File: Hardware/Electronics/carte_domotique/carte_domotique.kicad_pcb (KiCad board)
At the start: 2 copper layers, 27.9 x 58.4 mm, 3 parts, among them J1 Conn_02x08_Counter_Clockwise, J2 Raspberry_Pi_2_3, J3 Conn_01x02

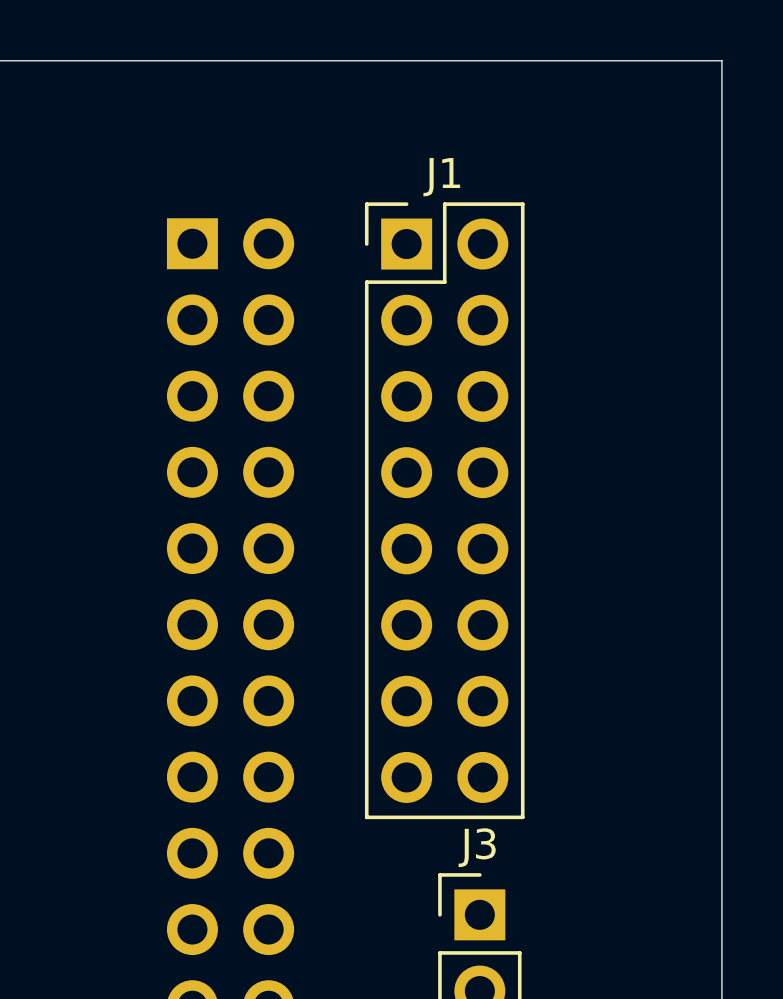
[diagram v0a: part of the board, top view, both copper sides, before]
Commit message: motification du conneteur pour le raspbee II
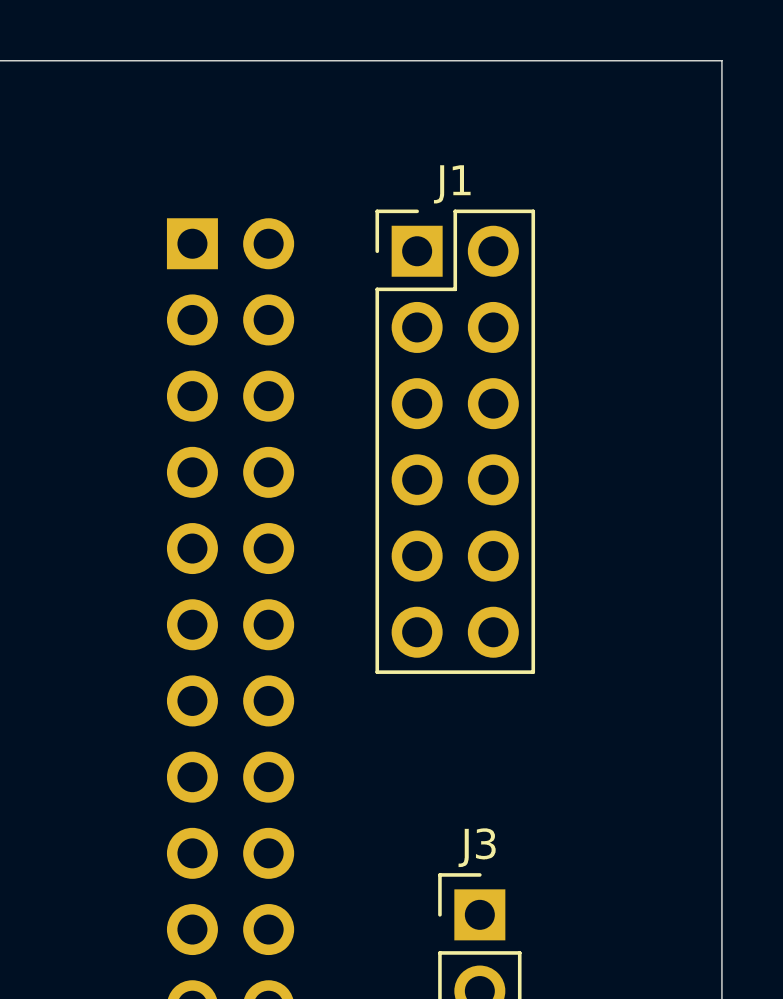
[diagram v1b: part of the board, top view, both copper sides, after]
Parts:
- J1: value Conn_02x08_Counter_Clockwise -> Conn_02x06_Odd_Even; footprint Connector_PinHeader_2.54mm:PinHeader_2x08_P2.54mm_Vertical -> Connector_PinHeader_2.54mm:PinHeader_2x06_P2.54mm_Vertical
- moved J1 0.42 mm to (147.3, 39.4)
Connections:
- J1 pad 5: Net-(J1-Pad10) -> Net-(J1-Pad5)
- J2 pad 10: Net-(J1-Pad12) -> Net-(J1-Pad10)
- J2 pad 11: Net-(J1-Pad6) -> Net-(J1-Pad11)
- J2 pad 12: Net-(J1-Pad11) -> Net-(J1-Pad12)
- J2 pad 13: Net-(J1-Pad7) -> Net-(J2-Pad13)
- J2 pad 14: Net-(J1-Pad10) -> Net-(J1-Pad9)
- J2 pad 15: Net-(J1-Pad8) -> Net-(J2-Pad15)
- J2 pad 16: Net-(J1-Pad9) -> Net-(J2-Pad16)
- J2 pad 2: Net-(J1-Pad15) -> Net-(J1-Pad2)
- J2 pad 20: Net-(J1-Pad10) -> Net-(J1-Pad9)
- J2 pad 25: Net-(J1-Pad10) -> Net-(J1-Pad9)
- J2 pad 3: Net-(J1-Pad2) -> Net-(J1-Pad3)
- J2 pad 30: Net-(J1-Pad10) -> Net-(J1-Pad9)
- J2 pad 34: Net-(J1-Pad10) -> Net-(J1-Pad9)
- J2 pad 39: Net-(J1-Pad10) -> Net-(J1-Pad9)
- J2 pad 4: Net-(J1-Pad15) -> Net-(J1-Pad2)
- J2 pad 5: Net-(J1-Pad3) -> Net-(J1-Pad5)
- J2 pad 6: Net-(J1-Pad10) -> Net-(J1-Pad9)
- J2 pad 7: Net-(J1-Pad4) -> Net-(J1-Pad7)
- J2 pad 8: Net-(J1-Pad13) -> Net-(J1-Pad8)
- J2 pad 9: Net-(J1-Pad10) -> Net-(J1-Pad9)
- J3 pad 1: Net-(J1-Pad15) -> Net-(J1-Pad2)
- J3 pad 2: Net-(J1-Pad10) -> Net-(J1-Pad6)

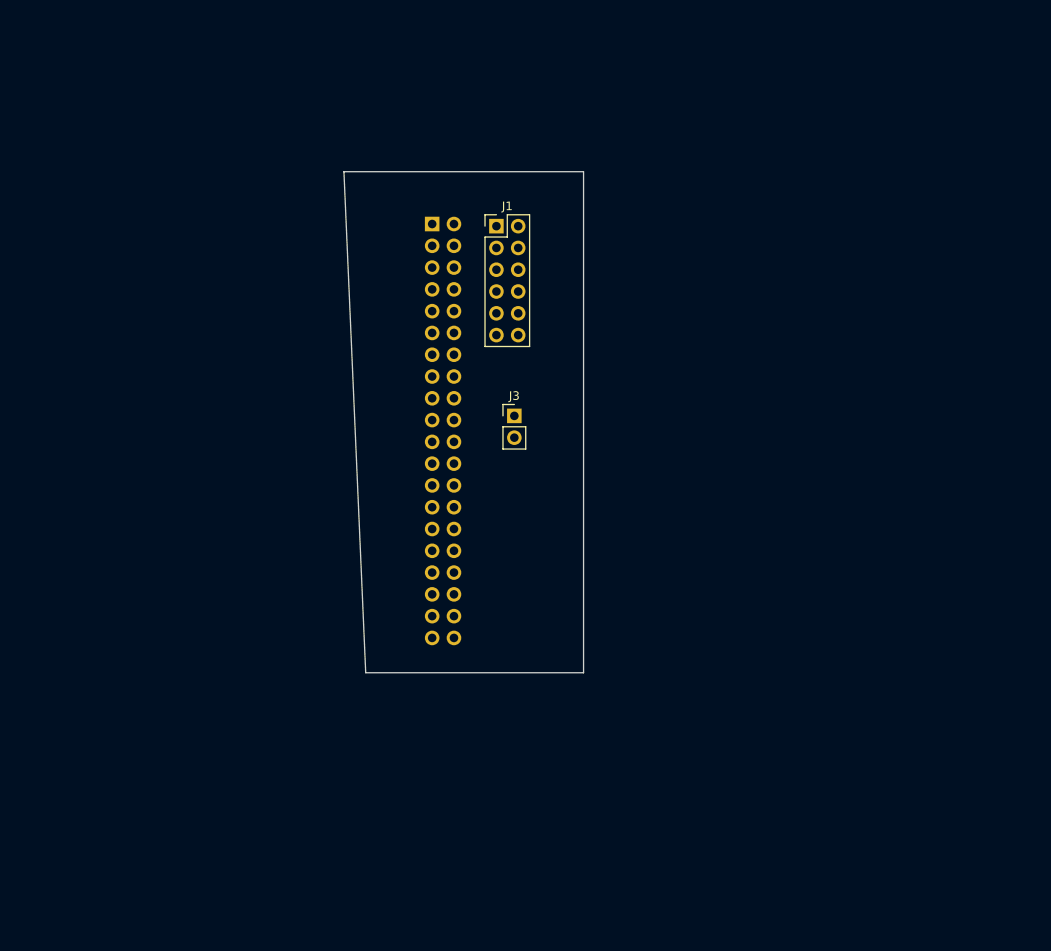
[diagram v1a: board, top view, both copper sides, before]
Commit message: kicad
schematic + empreinte
tracage des bus
+ mise en place des connecteur spi i2c pwm pcm 5v 33v gnd
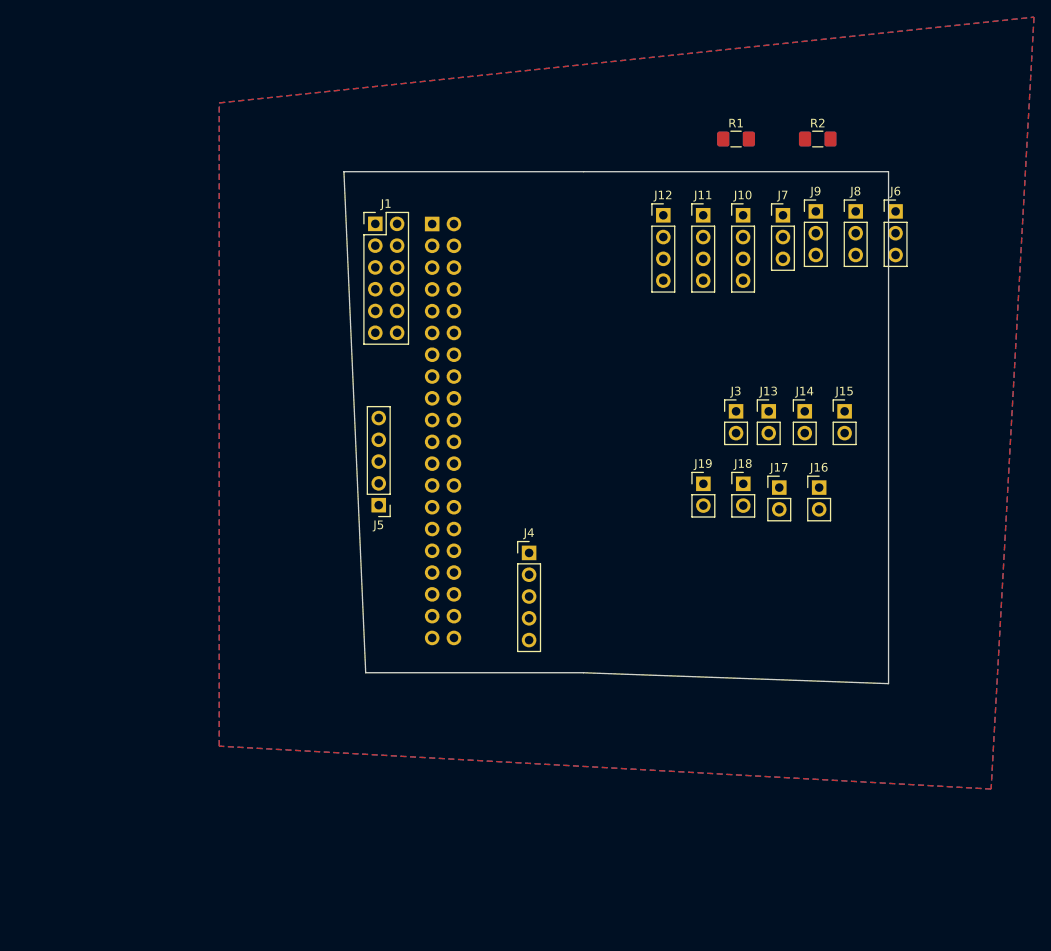
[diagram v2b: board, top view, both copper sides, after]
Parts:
- added J10: Conn_01x04, Connector_PinHeader_2.54mm:PinHeader_1x04_P2.54mm_Vertical, F.Cu at (176.1, 38.1)
- added J11: Conn_01x04, Connector_PinHeader_2.54mm:PinHeader_1x04_P2.54mm_Vertical, F.Cu at (171.4, 38.1)
- added J12: Conn_01x04, Connector_PinHeader_2.54mm:PinHeader_1x04_P2.54mm_Vertical, F.Cu at (166.8, 38.1)
- added J13: Conn_01x02, Connector_PinHeader_2.54mm:PinHeader_1x02_P2.54mm_Vertical, F.Cu at (179.1, 61.0)
- added J14: Conn_01x02, Connector_PinHeader_2.54mm:PinHeader_1x02_P2.54mm_Vertical, F.Cu at (183.3, 61.0)
- added J15: Conn_01x02, Connector_PinHeader_2.54mm:PinHeader_1x02_P2.54mm_Vertical, F.Cu at (187.9, 61.0)
- added J16: Conn_01x02, Connector_PinHeader_2.54mm:PinHeader_1x02_P2.54mm_Vertical, F.Cu at (184.9, 69.8)
- added J17: Conn_01x02, Connector_PinHeader_2.54mm:PinHeader_1x02_P2.54mm_Vertical, F.Cu at (180.3, 69.8)
- added J18: Conn_01x02, Connector_PinHeader_2.54mm:PinHeader_1x02_P2.54mm_Vertical, F.Cu at (176.1, 69.4)
- added J19: Conn_01x02, Connector_PinHeader_2.54mm:PinHeader_1x02_P2.54mm_Vertical, F.Cu at (171.4, 69.4)
- added J4: Conn_01x05, Connector_PinHeader_2.54mm:PinHeader_1x05_P2.54mm_Vertical, F.Cu at (151.1, 77.5)
- added J5: Conn_01x05, Connector_PinHeader_2.54mm:PinHeader_1x05_P2.54mm_Vertical, F.Cu at (133.6, 71.9)
- added J6: Conn_01x03, Connector_PinHeader_2.54mm:PinHeader_1x03_P2.54mm_Vertical, F.Cu at (193.9, 37.6)
- added J7: Conn_01x03, Connector_PinHeader_2.54mm:PinHeader_1x03_P2.54mm_Vertical, F.Cu at (180.7, 38.1)
- added J8: Conn_01x03, Connector_PinHeader_2.54mm:PinHeader_1x03_P2.54mm_Vertical, F.Cu at (189.2, 37.6)
- added J9: Conn_01x03, Connector_PinHeader_2.54mm:PinHeader_1x03_P2.54mm_Vertical, F.Cu at (184.6, 37.6)
- added R1: R, Resistor_SMD:R_1206_3216Metric_Pad1.42x1.75mm_HandSolder, F.Cu at (175.3, 29.2)
- added R2: R, Resistor_SMD:R_1206_3216Metric_Pad1.42x1.75mm_HandSolder, F.Cu at (184.8, 29.2)
- moved J3 25.9 mm to (175.3, 61.0)
- moved J1 14.1 mm to (133.2, 39.1)
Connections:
- net Net-(J1-Pad1) renamed +3V3
- net Net-(J1-Pad12) renamed /SW1
- J1 pad 11: Net-(J1-Pad11) -> reset
- J1 pad 4: Net-(J1-Pad4) -> Net-(J1-Pad2)
- J1 pad 6: Net-(J1-Pad6) -> GND
- J1 pad 9: Net-(J1-Pad9) -> GND
- J2 pad 11: Net-(J1-Pad11) -> Net-(J2-Pad11)
- J2 pad 14: Net-(J1-Pad9) -> GND
- J2 pad 20: Net-(J1-Pad9) -> GND
- J2 pad 25: Net-(J1-Pad9) -> GND
- J2 pad 3: Net-(J1-Pad3) -> SDA
- J2 pad 30: Net-(J1-Pad9) -> GND
- J2 pad 34: Net-(J1-Pad9) -> GND
- J2 pad 36: Net-(J2-Pad36) -> reset
- J2 pad 39: Net-(J1-Pad9) -> GND
- J2 pad 5: Net-(J1-Pad5) -> SCL
- J2 pad 6: Net-(J1-Pad9) -> GND
- J2 pad 7: Net-(J1-Pad7) -> Net-(J2-Pad7)
- J2 pad 9: Net-(J1-Pad9) -> GND
- J3 pad 1: Net-(J1-Pad2) -> +5V
- J3 pad 2: Net-(J1-Pad6) -> GND
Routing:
- added copper zone on B.Cu, net GND
- added copper zone on F.Cu, net GND
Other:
- board size 27.9 x 58.4 mm -> 63.5 x 59.7 mm

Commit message: carte 1
carte proto 1
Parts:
- R1, R2: moved to B.Cu
- moved J6 72.6 mm to (135.6, 80.9), turned to 180 degrees
- moved J2 70.0 mm to (176.9, 98.5), turned to 90 degrees
- moved J1 67.0 mm to (176.9, 89.9), turned to 270 degrees
- moved J7 65.1 mm to (131.7, 80.9), turned to 180 degrees
- moved J8 62.8 mm to (143.7, 81.0), turned to 180 degrees
- moved J9 62.4 mm to (139.6, 81.0), turned to 180 degrees
- moved R2 46.1 mm to (157.0, 65.9), turned to 90 degrees
- moved J12 44.0 mm to (151.9, 79.5), turned to 90 degrees
- moved R1 42.2 mm to (154.4, 66.0), turned to 90 degrees
- moved J16 41.9 mm to (143.2, 67.2), turned to 270 degrees
- moved J11 41.7 mm to (151.9, 74.9), turned to 90 degrees
- moved J10 40.2 mm to (151.9, 70.2), turned to 90 degrees
- moved J17 37.7 mm to (143.2, 63.4), turned to 270 degrees
- moved J18 34.4 mm to (143.1, 59.5), turned to 270 degrees
- moved J19 31.5 mm to (143.1, 55.6), turned to 270 degrees
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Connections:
- J1 pad 2: Net-(J1-Pad2) -> +5V
- J1 pad 4: Net-(J1-Pad2) -> +5V
- J2 pad 11: Net-(J2-Pad11) -> reset
- J2 pad 2: Net-(J1-Pad2) -> +5V
- J2 pad 36: reset -> Net-(J2-Pad36)
- J2 pad 4: Net-(J1-Pad2) -> +5V
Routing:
- net +5V: track 0.00 -> 163.5 mm
- net +3V3: track 0.00 -> 88.2 mm
- net SDA: track 0.00 -> 42.9 mm
- net SCL: track 0.00 -> 42.2 mm
- net Net-(J2-Pad33): track 0.00 -> 31.0 mm
- net Net-(J2-Pad32): track 0.00 -> 29.0 mm
- net Net-(J2-Pad28): track 0.00 -> 26.7 mm
- net GND: track 0.00 -> 23.9 mm
- net Net-(J2-Pad27): track 0.00 -> 22.6 mm
- net Net-(J2-Pad40): track 0.00 -> 12.5 mm
- net Net-(J2-Pad38): track 0.00 -> 12.4 mm
- net /SW1: track 0.00 -> 10.1 mm
- net Net-(J1-Pad8): track 0.00 -> 9.57 mm
- net Net-(J1-Pad10): track 0.00 -> 9.54 mm
- net reset: track 0.00 -> 9.54 mm
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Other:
- board size 63.5 x 59.7 mm -> 66 x 63.5 mm

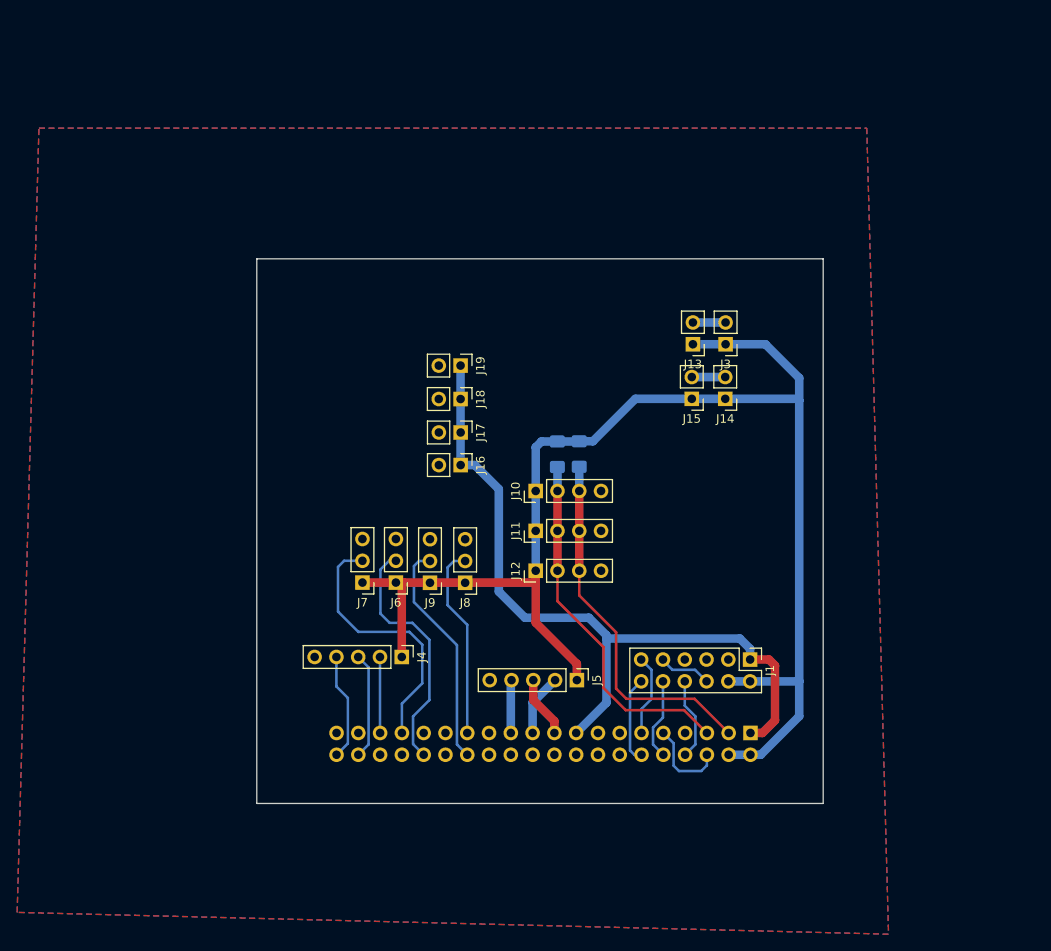
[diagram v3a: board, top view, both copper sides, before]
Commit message: carte electronique
finalisation de la carte électronique
+ exportation 3D
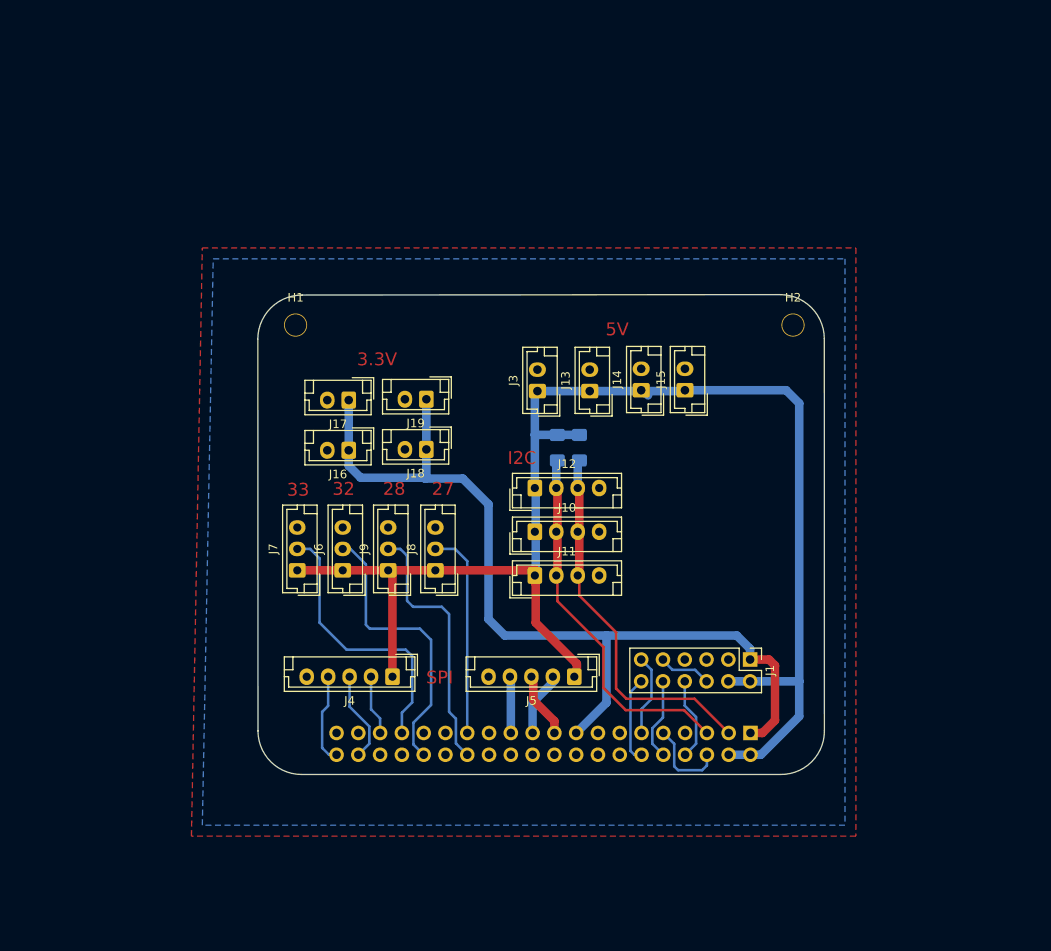
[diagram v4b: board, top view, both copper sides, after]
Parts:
- added H1: MountingHole_Pad, MountingHole:MountingHole_2.2mm_M2, F.Cu at (123.9, 50.9)
- added H2: MountingHole_Pad, MountingHole:MountingHole_2.2mm_M2, F.Cu at (181.9, 50.9)
- J10, J11, J12: footprint Connector_PinHeader_2.54mm:PinHeader_1x04_P2.54mm_Vertical -> Connector_JST:JST_EH_B4B-EH-A_1x04_P2.50mm_Vertical
- J13, J14, J15, J16, J17, J18, J19, J3: footprint Connector_PinHeader_2.54mm:PinHeader_1x02_P2.54mm_Vertical -> Connector_JST:JST_EH_B2B-EH-A_1x02_P2.50mm_Vertical
- J4, J5: footprint Connector_PinHeader_2.54mm:PinHeader_1x05_P2.54mm_Vertical -> Connector_JST:JST_EH_B5B-EH-A_1x05_P2.50mm_Vertical
- J6, J7, J8, J9: footprint Connector_PinHeader_2.54mm:PinHeader_1x03_P2.54mm_Vertical -> Connector_JST:JST_EH_B3B-EH-A_1x03_P2.50mm_Vertical
- moved J3 22.6 mm to (152.1, 58.6), turned to 90 degrees
- moved J17 13.6 mm to (130.1, 59.6), turned to 180 degrees
- moved J13 13.2 mm to (158.2, 58.6), turned to 90 degrees
- moved J16 13.2 mm to (130.1, 65.5), turned to 180 degrees
- moved J14 9.85 mm to (164.2, 58.5), turned to 90 degrees
- moved J12 9.65 mm to (151.8, 69.9), turned to 0 degrees
- moved J7 7.73 mm to (124.1, 79.5), turned to 90 degrees
- moved J18 7.10 mm to (139.2, 65.4), turned to 180 degrees
- moved J6 6.36 mm to (129.4, 79.5), turned to 90 degrees
- moved J19 5.60 mm to (139.2, 59.5), turned to 180 degrees
- moved J11 5.21 mm to (151.8, 80.1), turned to 0 degrees
- moved J9 5.09 mm to (134.7, 79.5), turned to 90 degrees
- moved J10 4.76 mm to (151.8, 75.0), turned to 0 degrees
- moved J8 3.77 mm to (140.2, 79.5), turned to 90 degrees
- moved J4 2.54 mm to (135.2, 91.9), turned to 180 degrees
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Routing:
- net +3V3: track 88.2 -> 107.6 mm
- net GND: track 23.9 -> 16.1 mm
- net +5V: track 163.5 -> 168.1 mm
- net Net-(J2-Pad32): track 29.0 -> 33.0 mm
- net Net-(J2-Pad28): track 26.7 -> 29.9 mm
- net Net-(J2-Pad40): track 12.5 -> 10.6 mm
- net Net-(J2-Pad35): track 8.87 -> 7.02 mm
- net Net-(J2-Pad38): track 12.4 -> 10.6 mm
- net Net-(J2-Pad27): track 22.6 -> 23.7 mm
- net Net-(J2-Pad33): track 31.0 -> 31.8 mm
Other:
- board size 66 x 63.5 mm -> 66.1 x 55.9 mm
- board text added: "27"
- board text added: "28"
- board text added: "3.3V"
- board text added: "32"
- board text added: "33"
- board text added: "5V"
- board text added: "I2C"
- board text added: "SPI"
